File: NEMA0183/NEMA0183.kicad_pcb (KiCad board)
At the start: 2 copper layers, 50.8 x 22.9 mm, 34 parts, among them J1 U.FL-R-SMT-1(01), J2 Feather_Top_Female, J3 Feather_Bottom_Female, Q1 MMBTH10-4L, U1 SA636DK

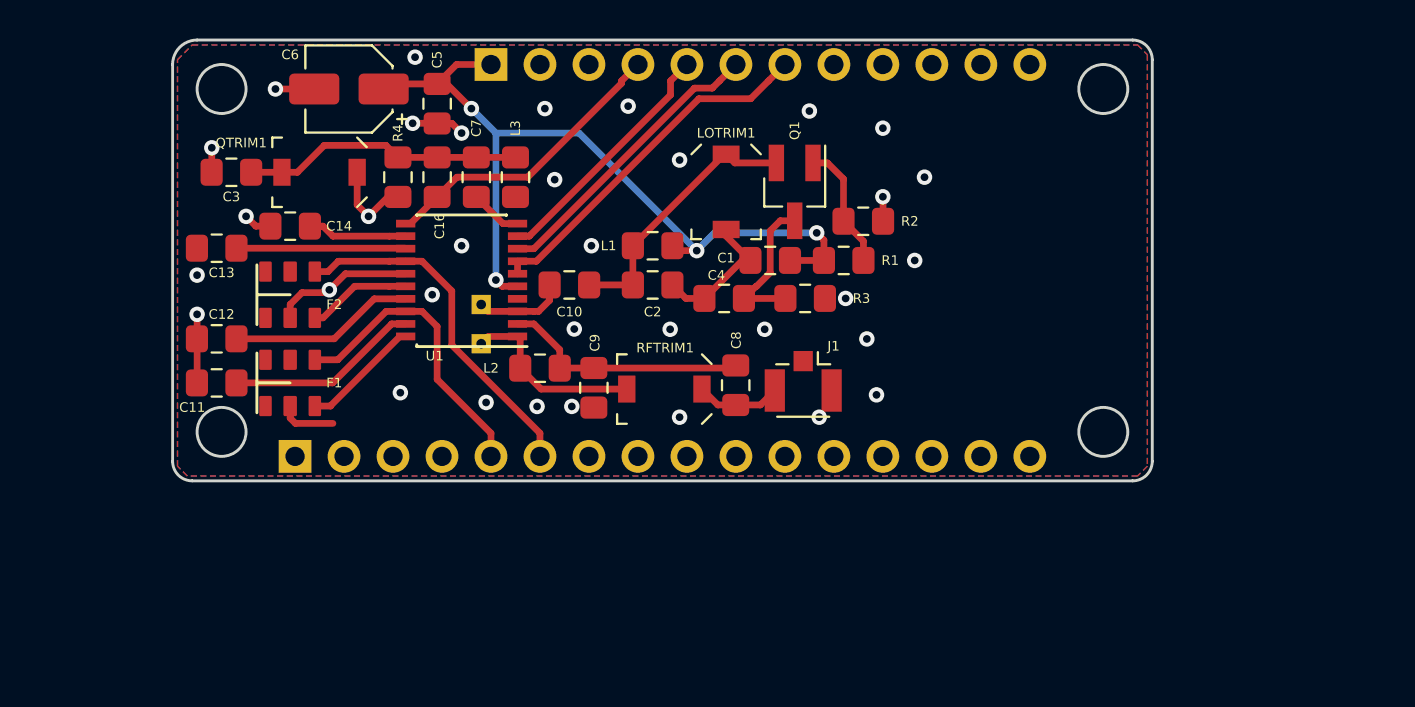
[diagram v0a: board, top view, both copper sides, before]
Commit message: More PCB work on AIS Feather receiver
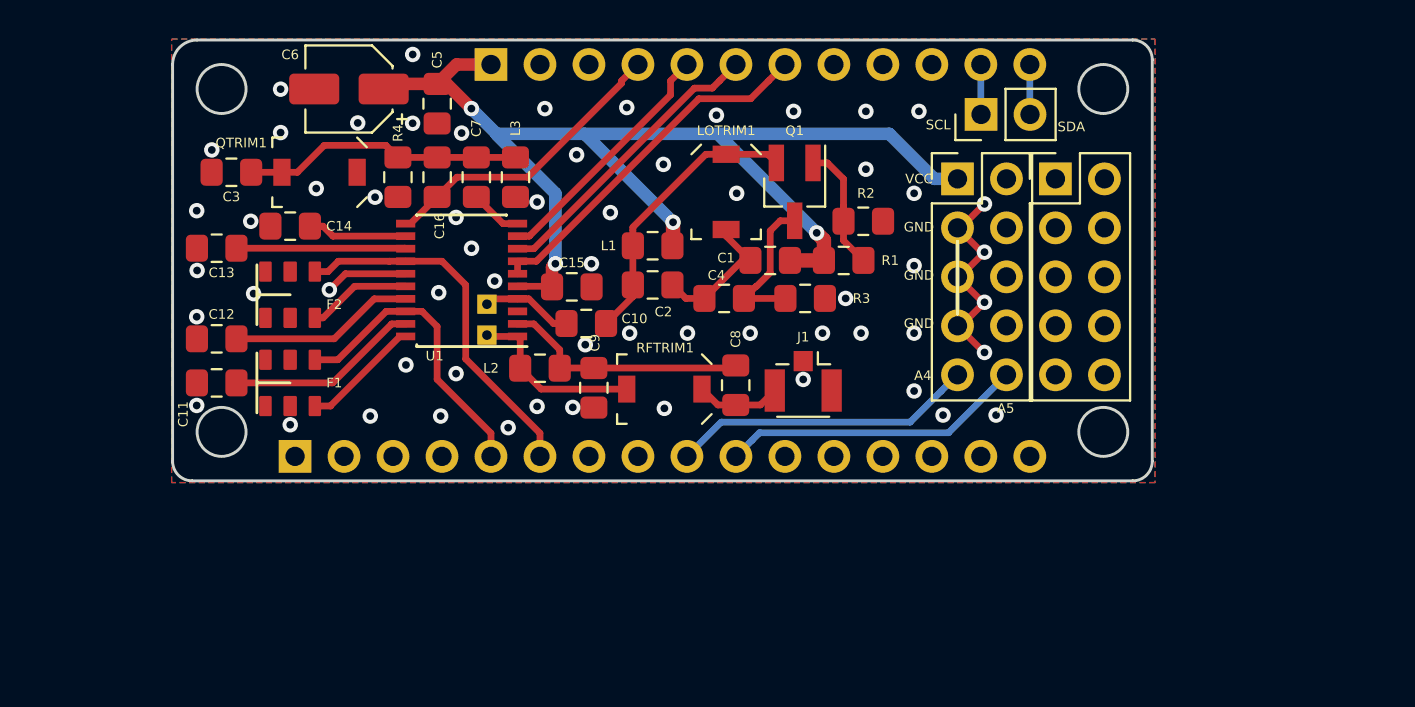
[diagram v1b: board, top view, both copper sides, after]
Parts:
- removed LO1: TestPoint, TestPoint:TestPoint_THTPad_1.0x1.0mm_Drill0.5mm
- added BB3: Conn_01x02_Female, Connector_PinHeader_2.54mm:PinHeader_1x02_P2.54mm_Vertical, F.Cu at (92.7, 54.7)
- added C15: 100n, Capacitor_SMD:C_0805_2012Metric_Pad1.15x1.40mm_HandSolder, F.Cu at (71.5, 63.6)
- added LO2: TestPoint, TestPoint:TestPoint_THTPad_1.0x1.0mm_Drill0.5mm, B.Cu at (67.1, 64.5)
- added REF**: PinHeader_2x05_P2.54mm_Vertical, Connector_PinHeader_2.54mm:PinHeader_2x05_P2.54mm_Vertical, F.Cu at (96.6, 58.0)
- added REF**: PinHeader_2x05_P2.54mm_Vertical, Connector_PinHeader_2.54mm:PinHeader_2x05_P2.54mm_Vertical, F.Cu at (91.5, 58.0)
- L2: value L_Core_Iron -> L
- moved C10 2.18 mm to (72.2, 65.5)
- moved RF1 0.54 mm to (67.1, 66.1)
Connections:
- net Net-(C16-Pad1) renamed /LIM_OUT
- net Net-(F1-Pad6) renamed /IF_AMP_IN
- net Net-(F2-Pad6) renamed /LIM_IN
- net Net-(J2-Pad07) renamed /POW_CON
- net Net-(J2-Pad11) renamed /RSSI
- net Net-(J2-Pad15) renamed /DAT_OUT
- J2 pad SCL: (no net) -> /SCL
- J2 pad SDA: (no net) -> /SDA
- J3 pad A4: (no net) -> /A4
- J3 pad A5: (no net) -> /A5
- U1 pad 3: Net-(C10-Pad1) -> Net-(LO1-Pad1)
- U1 pad 4: (no net) -> Net-(C10-Pad1)
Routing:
- net VCC: track 43.3 -> 65.0 mm
- net /A4: track 0.00 -> 15.8 mm
- net /A5: track 0.00 -> 15.8 mm
- net Earth: track 26.9 -> 15.9 mm, vias 34 -> 60
- net /SDA: track 0.00 -> 2.59 mm
- net /SCL: track 0.00 -> 2.59 mm
- net Net-(C10-Pad2): track 14.1 -> 14.9 mm
- net /LIM_IN: track 18.4 -> 19.0 mm
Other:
- rule pad_to_mask_clearance: 0.2 -> 0.0508
- board text added: "A4"
- board text added: "A5"
- board text added: "GND"
- board text added: "SCL"
- board text added: "SDA"
- board text added: "VCC"

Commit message: Using Si5351 for LO
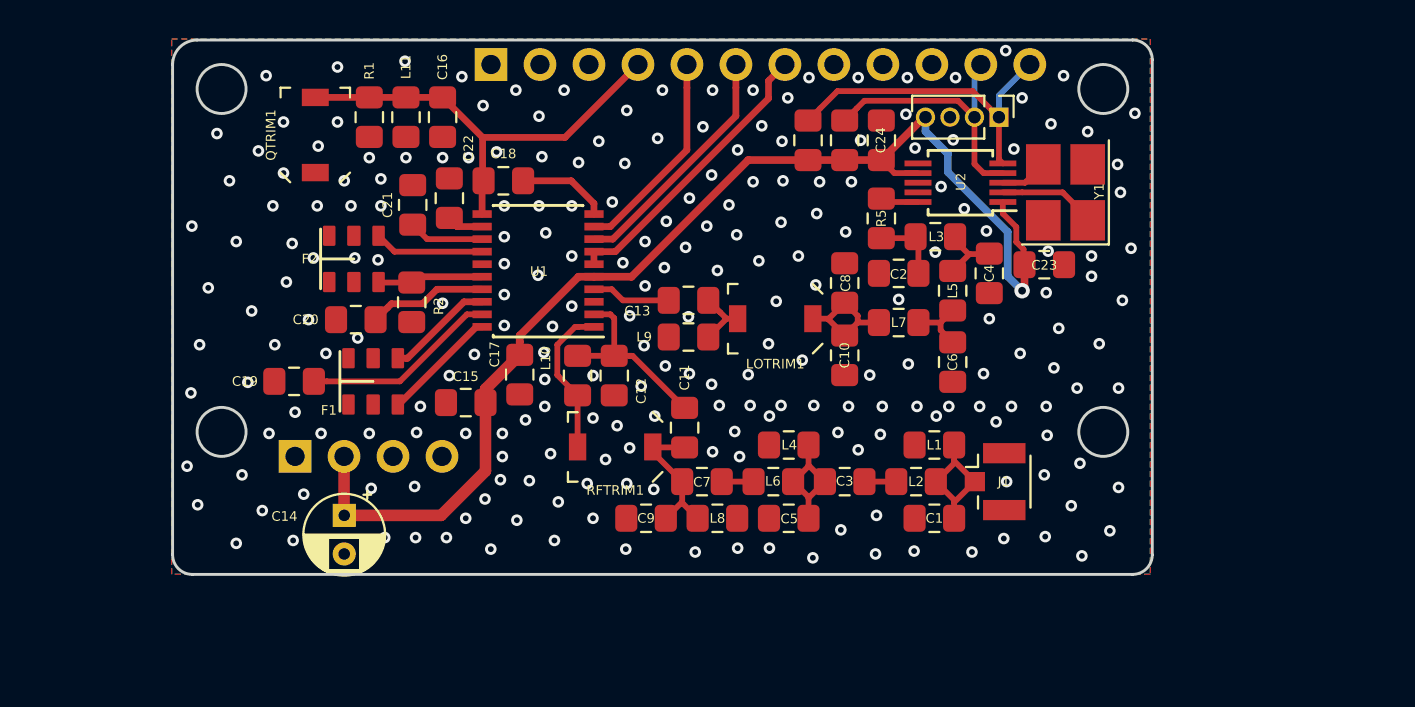
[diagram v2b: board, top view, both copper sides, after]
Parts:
- removed BB3: Conn_01x02_Female, Connector_PinHeader_2.54mm:PinHeader_1x02_P2.54mm_Vertical
- removed LO2, RF1: TestPoint, TestPoint:TestPoint_THTPad_1.0x1.0mm_Drill0.5mm
- removed Q1: MMBTH10-4L, Package_TO_SOT_SMD:SOT-23_Handsoldering
- removed REF** (x2): PinHeader_2x05_P2.54mm_Vertical, Connector_PinHeader_2.54mm:PinHeader_2x05_P2.54mm_Vertical
- added C17: 100n, Capacitor_SMD:C_0805_2012Metric_Pad1.15x1.40mm_HandSolder, F.Cu at (68.8, 68.2)
- added C18: C, Capacitor_SMD:C_0805_2012Metric_Pad1.15x1.40mm_HandSolder, F.Cu at (68.0, 58.1)
- added C19: 10nF, Capacitor_SMD:C_0805_2012Metric_Pad1.15x1.40mm_HandSolder, F.Cu at (57.1, 68.5)
- added C20: 10nF, Capacitor_SMD:C_0805_2012Metric_Pad1.15x1.40mm_HandSolder, F.Cu at (60.3, 65.3)
- added C21: 10nF, Capacitor_SMD:C_0805_2012Metric_Pad1.15x1.40mm_HandSolder, F.Cu at (63.2, 59.4)
- added C22: 10nF, Capacitor_SMD:C_0805_2012Metric_Pad1.15x1.40mm_HandSolder, F.Cu at (65.2, 59.0)
- added C23: 100n, Capacitor_SMD:C_0805_2012Metric_Pad1.15x1.40mm_HandSolder, F.Cu at (96.0, 62.5)
- added C24: 100n, Capacitor_SMD:C_0805_2012Metric_Pad1.15x1.40mm_HandSolder, F.Cu at (87.5, 56.0)
- added J4: Conn_01x02_Female, Connector_PinHeader_1.27mm:PinHeader_1x04_P1.27mm_Vertical, F.Cu at (93.7, 54.8)
- added L10: L, Inductor_SMD:L_0805_2012Metric_Pad1.15x1.40mm_HandSolder, F.Cu at (71.8, 68.2)
- added L11: L, Inductor_SMD:L_0805_2012Metric_Pad1.15x1.40mm_HandSolder, F.Cu at (62.9, 54.8)
- added L4: 3.6n, Inductor_SMD:L_0805_2012Metric_Pad1.15x1.40mm_HandSolder, F.Cu at (82.8, 71.8)
- added L5: 82n, Inductor_SMD:L_0805_2012Metric_Pad1.15x1.40mm_HandSolder, F.Cu at (91.2, 63.8)
- added L6: 560n, Inductor_SMD:L_0805_2012Metric_Pad1.15x1.40mm_HandSolder, F.Cu at (82.0, 73.7)
- added L7: 68n, Inductor_SMD:L_0805_2012Metric_Pad1.15x1.40mm_HandSolder, F.Cu at (88.5, 65.5)
- added L8: 11n, Inductor_SMD:L_0805_2012Metric_Pad1.15x1.40mm_HandSolder, F.Cu at (79.0, 75.6)
- added L9: L, Inductor_SMD:L_0805_2012Metric_Pad1.15x1.40mm_HandSolder, F.Cu at (77.5, 66.2)
- added R5: 0, Resistor_SMD:R_0805_2012Metric_Pad1.15x1.40mm_HandSolder, F.Cu at (87.5, 60.0)
- added U2: SI5351A, Package_SO:MSOP-10_3x3mm_P0.5mm, F.Cu at (91.7, 58.2)
- added Y1: Crystal_GND24, Crystal:Crystal_SMD_3225-4Pin_3.2x2.5mm_HandSoldering, F.Cu at (97.1, 58.7)
- C1: value C -> 82p
- C10: value 10n -> C
- C11: value 10nF -> C
- C12, C13: value 10nF -> 10n
- C14: value 10nF -> 68u; footprint Capacitor_SMD:C_0805_2012Metric_Pad1.15x1.40mm_HandSolder -> Capacitor_THT:CP_Radial_D4.0mm_P2.00mm
- C2, C8: value C -> 15p
- C3, C7: value C -> 1.7p
- C4: value 10n -> 36p
- C5: value 100n -> 270p
- C6: value UCL1E100MCL1GS -> 36p; footprint Capacitor_SMD:CP_Elec_4x5.8 -> Capacitor_SMD:C_0805_2012Metric_Pad1.15x1.40mm_HandSolder
- C9: value 10n -> 82p
- J3: footprint Adafruit:PinHeader_Adafruit_Feather_Bottom -> Connector_PinHeader_2.54mm:PinHeader_1x04_P2.54mm_Vertical
- L1: value L -> 11n
- L2: value L -> 560n
- L3: value L -> 68n
- R2: value R -> 120
- R3, R4: value R -> 4.7k
- moved C3 35.6 mm to (85.7, 73.7), turned to 0 degrees
- moved C6 34.4 mm to (91.2, 67.5), turned to 270 degrees
- moved C5 28.2 mm to (82.8, 75.6), turned to 180 degrees
- moved R1 25.7 mm to (61.0, 54.8), turned to 270 degrees
- moved C13 24.6 mm to (77.5, 64.3), turned to 180 degrees
- moved C11 24.4 mm to (77.3, 70.9), turned to 270 degrees
- moved R2 23.8 mm to (63.2, 64.4), turned to 270 degrees
- moved L3 22.0 mm to (90.3, 61.0), turned to 0 degrees
- moved R4 21.4 mm to (83.8, 56.0)
- moved C12 20.7 mm to (73.7, 68.2), turned to 90 degrees
- moved L2 20.4 mm to (89.3, 73.7), turned to 180 degrees
- moved C7 19.7 mm to (78.2, 73.7), turned to 0 degrees
- moved L1 17.9 mm to (90.3, 71.8)
- moved C1 15.8 mm to (90.3, 75.6)
- moved C14 15.3 mm to (59.7, 75.5), turned to 270 degrees
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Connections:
- net /POW_CON renamed /POW_CON_IN
- net /RSSI renamed /RSSI_OUT
- C1 pad 1: VCC -> Net-(C1-Pad1)
- C1 pad 2: Net-(C1-Pad2) -> Earth
- C10 pad 2: Net-(C10-Pad2) -> Earth
- C11 pad 1: Earth -> Net-(C11-Pad1)
- C12 pad 2: Net-(C12-Pad2) -> Net-(C11-Pad1)
- C13 pad 1: Earth -> Net-(C13-Pad1)
- C14 pad 1: Earth -> /3V3
- C14 pad 2: Net-(C14-Pad2) -> Earth
- C15 pad 1: VCC -> /3V3
- C16 pad 2: Net-(C16-Pad2) -> Earth
- C2 pad 1: Net-(C1-Pad2) -> /LO_IN
- C2 pad 2: Net-(C10-Pad2) -> Earth
- C3 pad 1: Net-(C16-Pad2) -> Net-(C3-Pad1)
- C3 pad 2: Earth -> Net-(C3-Pad2)
- C4 pad 1: Net-(C1-Pad2) -> Net-(C4-Pad1)
- C4 pad 2: Net-(C4-Pad2) -> Earth
- C5 pad 1: VCC -> Net-(C3-Pad1)
- C6 pad 1: VCC -> Net-(C6-Pad1)
- C7 pad 1: Net-(C16-Pad2) -> Net-(C11-Pad2)
- C8 pad 1: Net-(C8-Pad1) -> Net-(C10-Pad1)
- C8 pad 2: Net-(C8-Pad2) -> Earth
- C9 pad 1: Earth -> Net-(C11-Pad2)
- C9 pad 2: Net-(C8-Pad1) -> Earth
- F1 pad 6: /IF_AMP_IN -> Net-(F1-Pad6)
- F2 pad 6: /LIM_IN -> Net-(F2-Pad6)
- J1 pad 1: Earth -> Net-(C1-Pad1)
- J1 pad 2: Net-(C8-Pad2) -> Earth
- J2 pad BAT: VCC -> (no net)
- L1 pad 1: VCC -> Net-(C1-Pad1)
- L1 pad 2: Net-(C10-Pad2) -> Earth
- L2 pad 1: Net-(L2-Pad1) -> Net-(C1-Pad1)
- L2 pad 2: Net-(C8-Pad1) -> Net-(C3-Pad2)
- L3 pad 1: Net-(C16-Pad2) -> /LO_IN
- L3 pad 2: Earth -> Net-(C4-Pad1)
- LOTRIM1 pad 1: Net-(C10-Pad2) -> Net-(C10-Pad1)
- LOTRIM1 pad 2: Net-(C1-Pad2) -> Net-(C13-Pad1)
- QTRIM1 pad 2: Net-(C16-Pad2) -> /LIM_OUT
- R1 pad 1: VCC -> /LIM_OUT
- R1 pad 2: Net-(Q1-Pad1) -> Earth
- R2 pad 1: Net-(Q1-Pad1) -> Net-(F2-Pad1)
- R3 pad 1: Net-(C4-Pad2) -> /SCL
- R3 pad 2: Earth -> /3V3
- R4 pad 1: Net-(C16-Pad2) -> /SDA
- R4 pad 2: Earth -> /3V3
- RFTRIM1 pad 1: Net-(C8-Pad2) -> Net-(C11-Pad2)
- RFTRIM1 pad 2: Net-(L2-Pad1) -> Net-(L10-Pad1)
- U1 pad 1: Net-(L2-Pad1) -> Net-(L10-Pad1)
- U1 pad 10: Net-(C7-Pad2) -> Net-(C18-Pad2)
- U1 pad 12: Net-(C14-Pad2) -> Net-(C22-Pad2)
- U1 pad 13: Net-(C13-Pad2) -> Net-(C21-Pad2)
- U1 pad 14: /LIM_IN -> Net-(F2-Pad6)
- U1 pad 17: Net-(C12-Pad2) -> Net-(C20-Pad2)
- U1 pad 18: /IF_AMP_IN -> Net-(F1-Pad6)
- U1 pad 19: Net-(C11-Pad2) -> Net-(C19-Pad2)
- U1 pad 2: Net-(C8-Pad1) -> Net-(C11-Pad1)
- U1 pad 3: Net-(LO1-Pad1) -> (no net)
- U1 pad 4: Net-(C10-Pad1) -> Net-(C13-Pad2)
- U1 pad 5: VCC -> /3V3
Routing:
- net VCC: track 65.0 -> 0.00 mm, vias 4 -> 0
- net /3V3: track 0.00 -> 63.2 mm, vias 0 -> 1
- net /LIM_IN: track 19.0 -> 0.00 mm
- net Earth: track 15.9 -> 0.00 mm, vias 60 -> 227
- net /A4: track 15.8 -> 0.00 mm
- net /A5: track 15.8 -> 0.00 mm
- net /IF_AMP_IN: track 15.6 -> 0.00 mm
- net Net-(C10-Pad2): track 14.9 -> 0.00 mm
- net Net-(C16-Pad2): track 14.5 -> 0.00 mm
- net /SDA: track 2.59 -> 17.0 mm
- net Net-(C8-Pad1): track 12.9 -> 0.00 mm
- net /SCL: track 2.59 -> 14.5 mm
- net Net-(C19-Pad2): track 0.00 -> 10.2 mm
- net Net-(C11-Pad1): track 0.00 -> 9.75 mm
- net Net-(C12-Pad2): track 9.63 -> 0.00 mm
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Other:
- board size 50.8 x 22.9 mm -> 50.8 x 27.7 mm
- net class Default: trace_width 0.35 -> 0.3
- board text removed: "A4"
- board text removed: "A5"
- board text removed: "GND"
- board text removed: "SCL"
- board text removed: "SDA"
- board text removed: "VCC"

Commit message: NEMA0183
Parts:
- removed J4: Conn_01x02_Female, Connector_PinHeader_1.27mm:PinHeader_1x04_P1.27mm_Vertical
- removed LOTRIM1: LO TRIM, Capacitor_SMD:C_Trimmer_Voltronics_JZ
- removed R4: 4.7k, Resistor_SMD:R_0805_2012Metric_Pad1.15x1.40mm_HandSolder
- added JP1: Quad_Disable, Jumper:SolderJumper-2_P1.3mm_Bridged_RoundedPad1.0x1.5mm, F.Cu at (67.3, 56.9)
- added SCL_R1: 4.7k, Resistor_SMD:R_0805_2012Metric_Pad1.15x1.40mm_HandSolder, F.Cu at (106.3, 82.6)
- added SDA_R1: 4.7k, Resistor_SMD:R_0805_2012Metric_Pad1.15x1.40mm_HandSolder, F.Cu at (99.7, 81.7)
- C1, C9: value 82p -> 140.5p
- C12, C13: value 10n -> 10nF
- C14: value 68u -> 100uF; footprint Capacitor_THT:CP_Radial_D4.0mm_P2.00mm -> Capacitor_THT:CP_Radial_D5.0mm_P2.00mm
- C15: value 100n -> 10nF
- C17, C23, C24: value 100n -> 100nF
- C3, C7: value 1.7p -> 1.051p
- C5: value 270p -> 454.7p
- F1, F2: value SFECF -> SFECF_10M7
- L1, L8: value 11n -> 6.882n
- L2, L6: value 560n -> 919.7n
- L4: value 3.6n -> 2.127n
- R3: value 4.7k -> 120
- moved C15 46.2 mm to (111.5, 77.7), turned to 0 degrees
- moved C19 9.22 mm to (48.7, 72.3)
- moved F1 5.38 mm to (55.9, 67.6), turned to 270 degrees
- moved L8 3.70 mm to (75.3, 75.6), turned to 180 degrees
- moved C18 3.65 mm to (71.6, 58.2)
- moved F2 3.31 mm to (57.0, 61.3), turned to 270 degrees
- moved R2 3.06 mm to (61.3, 62.0), turned to 90 degrees
- moved C9 2.94 mm to (78.2, 76.5), turned to 270 degrees
- moved L4 2.25 mm to (85.0, 71.8), turned to 0 degrees
- moved C5 1.35 mm to (83.8, 76.5), turned to 270 degrees
- moved C1 1.27 mm to (91.2, 76.5), turned to 270 degrees
- moved L1 1.27 mm to (91.2, 71.0), turned to 90 degrees
- moved C6 1.27 mm to (92.2, 66.6), turned to 0 degrees
- moved C17 0.87 mm to (68.0, 67.8), turned to 225 degrees
- moved C20 0.81 mm to (61.1, 65.4)
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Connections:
- C12 pad 2: Net-(C11-Pad1) -> Net-(C11-Pad2)
- C15 pad 1: /3V3 -> Net-(C10-Pad1)
- C15 pad 2: Earth -> Net-(C13-Pad1)
- C16 pad 1: /LIM_OUT -> Net-(C16-Pad1)
- C18 pad 1: /LIM_OUT -> Net-(C16-Pad1)
- C7 pad 1: Net-(C11-Pad2) -> Net-(C11-Pad1)
- C9 pad 1: Net-(C11-Pad2) -> Net-(C11-Pad1)
- F1 pad 5: (no net) -> Earth
- F2 pad 5: (no net) -> Earth
- J2 pad SCL: /SCL -> Net-(J2-PadSCL)
- J2 pad SDA: /SDA -> Net-(J2-PadSDA)
- L10 pad 2: Net-(C11-Pad1) -> Net-(C11-Pad2)
- L11 pad 1: /LIM_OUT -> Net-(C16-Pad1)
- L8 pad 1: Net-(C11-Pad2) -> Net-(C11-Pad1)
- QTRIM1 pad 2: /LIM_OUT -> Net-(C16-Pad1)
- R1 pad 1: /LIM_OUT -> Net-(C16-Pad1)
- R2 pad 1: Net-(F2-Pad1) -> Net-(R2-Pad1)
- R3 pad 1: /SCL -> Net-(R2-Pad1)
- R3 pad 2: /3V3 -> Net-(F2-Pad1)
- RFTRIM1 pad 1: Net-(C11-Pad2) -> Net-(C11-Pad1)
- U1 pad 16: Net-(F2-Pad1) -> Net-(R2-Pad1)
- U1 pad 2: Net-(C11-Pad1) -> Net-(C11-Pad2)
- U2 pad 4: /SCL -> (no net)
- U2 pad 5: /SDA -> (no net)
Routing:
- net /SDA: track 17.0 -> 0.00 mm
- net Net-(C16-Pad1): track 0.00 -> 15.0 mm
- net /SCL: track 14.5 -> 0.00 mm
- net (no net): track 0.00 -> 13.6 mm
- net Net-(R2-Pad1): track 0.00 -> 10.6 mm
- net Net-(C19-Pad2): track 10.2 -> 0.00 mm
- net /LIM_OUT: track 23.1 -> 13.6 mm, vias 0 -> 1
- net Net-(C11-Pad2): track 7.53 -> 0.00 mm
- net /3V3: track 63.2 -> 55.9 mm
- net Net-(C11-Pad1): track 9.75 -> 3.97 mm
- net Net-(F2-Pad6): track 5.71 -> 0.01 mm
- net Net-(F2-Pad1): track 5.54 -> 0.00 mm
- net Net-(J2-PadSDA): track 0.00 -> 3.39 mm
- net Net-(C18-Pad2): track 4.76 -> 1.59 mm
- net Net-(J2-PadSCL): track 0.00 -> 2.87 mm
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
